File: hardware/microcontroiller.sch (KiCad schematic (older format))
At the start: 14 parts, among them J1 SWD, J2 USB_A, SW1 RESET Switch, U1 STM32L431CBTx, Y1 32.768kHz

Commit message: Finished MC design
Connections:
- net labels added: CP_SHDN_L, Charge_EN, Eh_Sense, MUX1_A0, MUX1_A1, MUX1_EN, MUX2_A0, MUX2_A1, MUX2_EN, Moisture_Sense, Ref_Elec, Temp_Sense
- wire segments 63 -> 79
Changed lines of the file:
@@
 L Device:C_Small C2
 U 1 1 6158D460
-P 3850 3850
-F 0 "C2" H 3900 3950 50  0000 L CNN
-F 1 "20pF" H 3900 3750 50  0000 L CNN
-F 2 "" H 3850 3850 50  0001 C CNN
-F 3 "~" H 3850 3850 50  0001 C CNN
-F 4 "399-C0603C200G4HAC7867CT-ND" H 3850 3850 50  0001 C CNN "Digikey"
-	1    3850 3850
+P 3750 3850
+F 0 "C2" H 3800 3950 50  0000 L CNN
+F 1 "20pF" H 3800 3750 50  0000 L CNN
+F 2 "" H 3750 3850 50  0001 C CNN
+F 3 "~" H 3750 3850 50  0001 C CNN
+F 4 "399-C0603C200G4HAC7867CT-ND" H 3750 3850 50  0001 C CNN "Digikey"
+	1    3750 3850
 	0    1    1    0
 $EndComp
@@
 L Device:C_Small C1
 U 1 1 6158E0B8
-P 3850 3650
-F 0 "C1" H 3750 3750 50  0000 L CNN
-F 1 "20pF" H 3600 3550 50  0000 L CNN
-F 2 "" H 3850 3650 50  0001 C CNN
-F 3 "~" H 3850 3650 50  0001 C CNN
-F 4 "399-C0603C200G4HAC7867CT-ND" H 3850 3650 50  0001 C CNN "Digikey"
-	1    3850 3650
+P 3750 3650
+F 0 "C1" H 3650 3750 50  0000 L CNN
+F 1 "20pF" H 3500 3550 50  0000 L CNN
+F 2 "" H 3750 3650 50  0001 C CNN
+F 3 "~" H 3750 3650 50  0001 C CNN
+F 4 "399-C0603C200G4HAC7867CT-ND" H 3750 3650 50  0001 C CNN "Digikey"
+	1    3750 3650
 	0    1    1    0
 $EndComp
 Wire Wire Line
-	4200 3650 3950 3650
+	4200 3650 3850 3650
 Connection ~ 4200 3650
 Wire Wire Line
-	4200 3850 3950 3850
+	4200 3850 3850 3850
 Connection ~ 4200 3850
 Wire Wire Line
-	3750 3850 3600 3850
-Wire Wire Line
-	3600 3850 3600 3750
-Wire Wire Line
-	3600 3650 3750 3650
+	3650 3850 3500 3850
+Wire Wire Line
+	3500 3850 3500 3750
+Wire Wire Line
+	3500 3650 3650 3650
 $Comp
 L power:GND #PWR06
 U 1 1 6158FD84
-P 3600 3750
-F 0 "#PWR06" H 3600 3500 50  0001 C CNN
-F 1 "GND" V 3605 3622 50  0000 R CNN
-F 2 "" H 3600 3750 50  0001 C CNN
-F 3 "" H 3600 3750 50  0001 C CNN
-	1    3600 3750
+P 3500 3750
+F 0 "#PWR06" H 3500 3500 50  0001 C CNN
+F 1 "GND" V 3505 3622 50  0000 R CNN
+F 2 "" H 3500 3750 50  0001 C CNN
+F 3 "" H 3500 3750 50  0001 C CNN
+	1    3500 3750
 	0    1    1    0
 $EndComp
-Connection ~ 3600 3750
-Wire Wire Line
-	3600 3750 3600 3650
+Connection ~ 3500 3750
+Wire Wire Line
+	3500 3750 3500 3650
 Text Label 5400 2750 2    50   ~ 0
 3V3_VDD
@@
 L Device:LED_Small D1
 U 1 1 6164F04D
-P 6300 4600
-F 0 "D1" H 6300 4835 50  0000 C CNN
-F 1 "Orange" H 6300 4744 50  0000 C CNN
-F 2 "" V 6300 4600 50  0001 C CNN
-F 3 "~" V 6300 4600 50  0001 C CNN
-F 4 "160-1413-1-ND" H 6300 4600 50  0001 C CNN "Digikey"
-	1    6300 4600
-	1    0    0    -1
-$EndComp
-Wire Wire Line
-	6200 4600 6000 4600
+P 4250 4400
+F 0 "D1" H 4250 4200 50  0000 C CNN
+F 1 "Orange" H 4250 4300 50  0000 C CNN
+F 2 "" V 4250 4400 50  0001 C CNN
+F 3 "~" V 4250 4400 50  0001 C CNN
+F 4 "160-1413-1-ND" H 4250 4400 50  0001 C CNN "Digikey"
+	1    4250 4400
+	-1   0    0    -1
+$EndComp
 $Comp
 L Device:R_Small R2
 U 1 1 61650FB5
-P 6700 4600
-F 0 "R2" V 6504 4600 50  0000 C CNN
-F 1 "680" V 6595 4600 50  0000 C CNN
-F 2 "" H 6700 4600 50  0001 C CNN
-F 3 "~" H 6700 4600 50  0001 C CNN
-F 4 "YAG3624CT-ND" V 6700 4600 50  0001 C CNN "Digikey"
-	1    6700 4600
-	0    1    1    0
-$EndComp
-Wire Wire Line
-	6600 4600 6400 4600
+P 3950 4400
+F 0 "R2" V 3850 4400 50  0000 C CNN
+F 1 "680" V 4050 4400 50  0000 C CNN
+F 2 "" H 3950 4400 50  0001 C CNN
+F 3 "~" H 3950 4400 50  0001 C CNN
+F 4 "YAG3624CT-ND" V 3950 4400 50  0001 C CNN "Digikey"
+	1    3950 4400
+	0    -1   -1   0
+$EndComp
+Wire Wire Line
+	4050 4400 4150 4400
 $Comp
 L power:+3V3 #PWR09
 U 1 1 61652B46
-P 6950 4600
-F 0 "#PWR09" H 6950 4450 50  0001 C CNN
-F 1 "+3V3" H 6965 4773 50  0000 C CNN
-F 2 "" H 6950 4600 50  0001 C CNN
-F 3 "" H 6950 4600 50  0001 C CNN
-	1    6950 4600
-	0    1    1    0
-$EndComp
-Wire Wire Line
-	6950 4600 6800 4600
+P 3800 4400
+F 0 "#PWR09" H 3800 4250 50  0001 C CNN
+F 1 "+3V3" H 3815 4573 50  0000 C CNN
+F 2 "" H 3800 4400 50  0001 C CNN
+F 3 "" H 3800 4400 50  0001 C CNN
+	1    3800 4400
+	0    -1   -1   0
+$EndComp
+Wire Wire Line
+	3800 4400 3850 4400
+Text GLabel 6100 4000 2    50   Input ~ 0
+Eh_Sense
+Text GLabel 6100 4100 2    50   Input ~ 0
+Temp_Sense
+Text GLabel 6100 4200 2    50   Input ~ 0
+Ref_Elec
+Text GLabel 6100 4300 2    50   Input ~ 0
+Moisture_Sense
+Text Label 6100 5100 0    50   ~ 0
+USB+
+Text Label 6100 5200 0    50   ~ 0
+USB-
+Wire Wire Line
+	6100 5100 6000 5100
+Wire Wire Line
+	6100 5200 6000 5200
+Text Label 6100 5300 0    50   ~ 0
+SWDIO
+Wire Wire Line
+	6100 5300 6000 5300
+Text Label 6100 5400 0    50   ~ 0
+SWCLK
+Wire Wire Line
+	6100 5400 6000 5400
+Text GLabel 6100 4400 2    50   Input ~ 0
+MUX1_EN
+Text GLabel 6100 4500 2    50   Input ~ 0
+MUX1_A0
+Text GLabel 6100 4600 2    50   Input ~ 0
+MUX1_A1
+Text GLabel 4700 4000 0    50   Input ~ 0
+MUX2_EN
+Wire Wire Line
+	6100 4000 6000 4000
+Wire Wire Line
+	6000 4100 6100 4100
+Wire Wire Line
+	6100 4200 6000 4200
+Wire Wire Line
+	6000 4300 6100 4300
+Wire Wire Line
+	6100 4400 6000 4400
+Wire Wire Line
+	6000 4500 6100 4500
+Wire Wire Line
+	6100 4600 6000 4600
+Text GLabel 4700 4100 0    50   Input ~ 0
+MUX2_A0
+Text GLabel 4700 4200 0    50   Input ~ 0
+MUX2_A1
+Wire Wire Line
+	4700 4000 4800 4000
+Wire Wire Line
+	4800 4100 4700 4100
+Wire Wire Line
+	4700 4200 4800 4200
+Wire Wire Line
+	4350 4400 4800 4400
+Text GLabel 4700 5000 0    50   Input ~ 0
+Charge_EN
+Text GLabel 4700 5100 0    50   Input ~ 0
+CP_SHDN_L
+$Comp
+L power:+5V #PWR?
+U 1 1 6162950C
+P 5600 2800
+F 0 "#PWR?" H 5600 2650 50  0001 C CNN
+F 1 "+5V" H 5615 2973 50  0000 C CNN
+F 2 "" H 5600 2800 50  0001 C CNN
+F 3 "" H 5600 2800 50  0001 C CNN
+	1    5600 2800
+	1    0    0    -1
+$EndComp
+Wire Wire Line
+	4800 5000 4700 5000
+Wire Wire Line
+	4700 5100 4800 5100
 $EndSCHEMATC

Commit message: Added 1V LDO. Added LDO symbol
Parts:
- U1: value STM32L431CBTx -> STM32L4Q5xx
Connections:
- net labels added: +1V0_EN
- wire segments 79 -> 80
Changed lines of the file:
@@
 P 5400 4200
 F 0 "U1" H 6050 5450 50  0000 C CNN
-F 1 "STM32L431CBTx" H 6250 5350 50  0000 C CNN
+F 1 "STM32L4Q5xx" H 6250 5350 50  0000 C CNN
 F 2 "Package_QFP:LQFP-48_7x7mm_P0.5mm" H 4900 2800 50  0001 R CNN
 F 3 "http://www.st.com/st-web-ui/static/active/en/resource/technical/document/datasheet/DM00257211.pdf" H 5400 4200 50  0001 C CNN
@@
 Wire Wire Line
 	4700 5100 4800 5100
+Text GLabel 4700 5200 0    50   Input ~ 0
++1V0_EN
+Wire Wire Line
+	4700 5200 4800 5200
 $EndSCHEMATC

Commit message: Not sure what changes I made sry
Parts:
- added C?: 0.1uF, symbol Device:C_Small
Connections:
- net labels removed: 3V3_VDD
- wire segments 80 -> 84
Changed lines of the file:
@@
 	4950 2300 4950 2350
 Connection ~ 4950 2350
-Wire Wire Line
-	4950 2350 4750 2350
 Connection ~ 4750 2050
 Wire Wire Line
@@
 Wire Wire Line
 	4550 2050 4750 2050
-Text Label 4750 2450 0    50   ~ 0
-3V3_VDD
-Wire Wire Line
-	4750 2450 4750 2350
-Connection ~ 4750 2350
-Wire Wire Line
-	4750 2350 4550 2350
 $Comp
 L Device:R_Small R1
@@
 Wire Wire Line
 	3500 3750 3500 3650
-Text Label 5400 2750 2    50   ~ 0
-3V3_VDD
 Wire Wire Line
 	5400 2800 5400 2750
@@
 F 1 "STM32L4Q5xx" H 6250 5350 50  0000 C CNN
 F 2 "Package_QFP:LQFP-48_7x7mm_P0.5mm" H 4900 2800 50  0001 R CNN
-F 3 "http://www.st.com/st-web-ui/static/active/en/resource/technical/document/datasheet/DM00257211.pdf" H 5400 4200 50  0001 C CNN
+F 3 "https://www.st.com/resource/en/datasheet/stm32l4q5ag.pdf" H 5400 4200 50  0001 C CNN
 F 4 "497-STM32L4Q5CGT6-ND" H 5400 4200 50  0001 C CNN "Digikey"
 	1    5400 4200
@@
 Text GLabel 4700 5100 0    50   Input ~ 0
 CP_SHDN_L
-$Comp
-L power:+5V #PWR?
-U 1 1 6162950C
-P 5600 2800
-F 0 "#PWR?" H 5600 2650 50  0001 C CNN
-F 1 "+5V" H 5615 2973 50  0000 C CNN
-F 2 "" H 5600 2800 50  0001 C CNN
-F 3 "" H 5600 2800 50  0001 C CNN
-	1    5600 2800
-	1    0    0    -1
-$EndComp
 Wire Wire Line
 	4800 5000 4700 5000
@@
 Wire Wire Line
 	4700 5200 4800 5200
+Wire Wire Line
+	4550 2350 4750 2350
+$Comp
+L power:+3V3 #PWR?
+U 1 1 615C7609
+P 5400 2750
+F 0 "#PWR?" H 5400 2600 50  0001 C CNN
+F 1 "+3V3" H 5415 2923 50  0000 C CNN
+F 2 "" H 5400 2750 50  0001 C CNN
+F 3 "" H 5400 2750 50  0001 C CNN
+	1    5400 2750
+	1    0    0    -1
+$EndComp
+$Comp
+L power:GND #PWR?
+U 1 1 615C81D2
+P 4750 2350
+F 0 "#PWR?" H 4750 2100 50  0001 C CNN
+F 1 "GND" H 4755 2177 50  0000 C CNN
+F 2 "" H 4750 2350 50  0001 C CNN
+F 3 "" H 4750 2350 50  0001 C CNN
+	1    4750 2350
+	1    0    0    -1
+$EndComp
+Connection ~ 4750 2350
+Wire Wire Line
+	4750 2350 4950 2350
+$Comp
+L Device:C_Small C?
+U 1 1 615C988A
+P 5550 2200
+F 0 "C?" H 5400 2250 50  0000 L CNN
+F 1 "0.1uF" H 5300 2100 50  0000 L CNN
+F 2 "" H 5550 2200 50  0001 C CNN
+F 3 "~" H 5550 2200 50  0001 C CNN
+F 4 "445-8122-1-ND" H 5550 2200 50  0001 C CNN "Digikey"
+	1    5550 2200
+	1    0    0    -1
+$EndComp
+Wire Wire Line
+	5550 2100 5550 2050
+Wire Wire Line
+	5550 2050 5250 2050
+Connection ~ 5250 2050
+Wire Wire Line
+	5550 2300 5550 2350
+Wire Wire Line
+	5550 2350 5250 2350
+Connection ~ 5250 2350
+Wire Wire Line
+	5600 2800 5500 2800
+Connection ~ 5500 2800
 $EndSCHEMATC

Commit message: House Keeping Tasks
 - Modified parts list parameters for various parts
 - Assigned Ref Des to components
 - Changed TPS717 symbol and feedback resistors
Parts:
- removed C2: 20pF, symbol Device:C_Small
- removed C4, C5, C6, C?: 0.1uF, symbol Device:C_Small
- added C?: 20pF, Capacitor_SMD:C_0603_1608Metric_Pad1.08x0.95mm_HandSolder, symbol Device:C_Small
- added C? (x4): 0.1uF, Capacitor_SMD:C_0603_1608Metric_Pad1.08x0.95mm_HandSolder, symbol Device:C_Small
- C1, C3: footprint (none) -> Capacitor_SMD:C_0603_1608Metric_Pad1.08x0.95mm_HandSolder
- D1: footprint (none) -> Resistor_SMD:R_0805_2012Metric_Pad1.20x1.40mm_HandSolder
- J2: footprint (none) -> Connector_USB:USB3_A_Molex_48393-001; symbol Connector:USB_A -> mallard-rescue:USB_A-Connector
- R1: footprint (none) -> Resistor_SMD:R_0201_0603Metric_Pad0.64x0.40mm_HandSolder
- R2: footprint (none) -> Resistor_SMD:R_0603_1608Metric_Pad0.98x0.95mm_HandSolder
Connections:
- wire segments 84 -> 85
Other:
- note added: "Double check footprint for USB connector"

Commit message: Added more ref des
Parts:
- gave numbers to parts that had none: 5
- renumbered C3 to C400, C1 to C405, R1 to R400, R2 to R401, SW1 to SW400, U1 to U400
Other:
- moved on the sheet: J2

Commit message: Finished adding TMP sensors and footprints
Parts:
- removed J1: SWD, symbol Connector_Generic:Conn_02x05_Odd_Even
- added J2: Conn_02x03_Odd_Even, Connector_PinHeader_1.27mm:PinHeader_2x03_P1.27mm_Vertical, symbol Connector_Generic:Conn_02x03_Odd_Even
- C1: renamed from C405; symbol Device:C_Small -> mallard-rescue:C_Small-Device
- C2: renamed from C400; symbol Device:C_Small -> mallard-rescue:C_Small-Device
- C3: renamed from C401; symbol Device:C_Small -> mallard-rescue:C_Small-Device
- C4: renamed from C406; symbol Device:C_Small -> mallard-rescue:C_Small-Device
- C5: renamed from C402; symbol Device:C_Small -> mallard-rescue:C_Small-Device
- C6: renamed from C403; symbol Device:C_Small -> mallard-rescue:C_Small-Device
- C7: renamed from C404; symbol Device:C_Small -> mallard-rescue:C_Small-Device
- D1: symbol Device:LED_Small -> mallard-rescue:LED_Small-Device
- R1: renamed from R401; symbol Device:R_Small -> mallard-rescue:R_Small-Device
- R2: renamed from R400; symbol Device:R_Small -> mallard-rescue:R_Small-Device
- SW1: renamed from SW400; footprint (none) -> Button_Switch_SMD:SW_SPST_B3U-1000P; symbol Switch:SW_Push_Open_Dual -> mallard-rescue:SW_Push_Open_Dual-Switch; Digikey (none) -> SW1020CT-ND
- U1: renamed from U400; symbol MCU_ST_STM32L4:STM32L431CBTx -> mallard-rescue:STM32L431CBTx-MCU_ST_STM32L4
- Y1: symbol Device:Crystal_Small -> mallard-rescue:Crystal_Small-Device
- renumbered J2 to J3
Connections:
- wire segments 85 -> 83
- no-connect marks 3 -> 1
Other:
- note added: "I have these switches on hand"
- note added: "Programming connector copied from a previous project (Flamingo)"

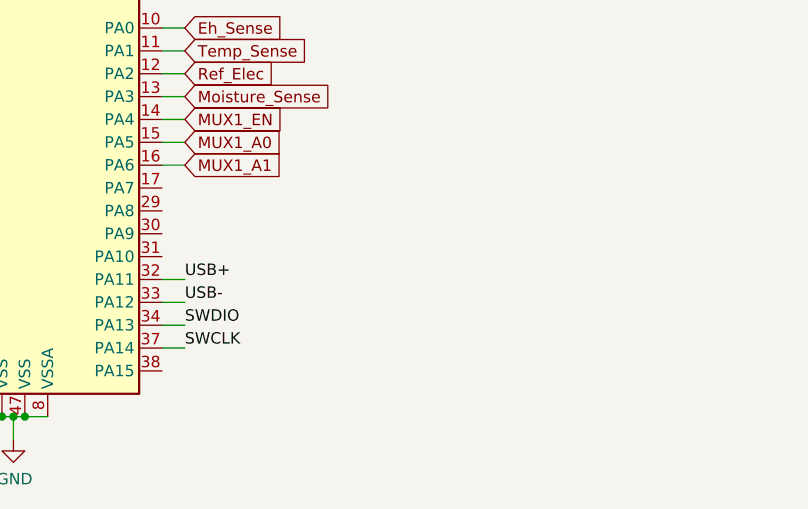
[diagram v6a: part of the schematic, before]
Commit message: Added UART connector on STM32
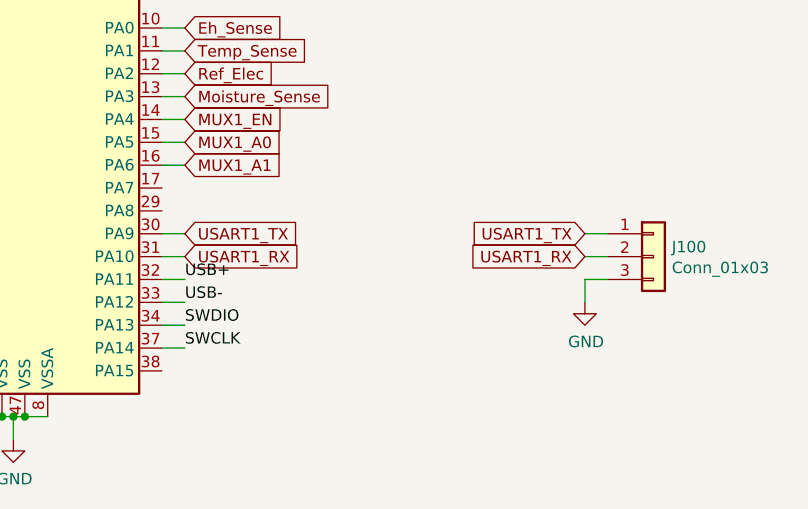
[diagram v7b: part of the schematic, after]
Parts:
- added J100: Conn_01x03, Connector_PinHeader_2.54mm:PinHeader_1x03_P2.54mm_Vertical_SMD_Pin1Right, symbol Connector_Generic:Conn_01x03
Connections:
- net GND: now also J100.3 (Pin_3)
- net USART1_TX: now reaches U1.30 (PA9)
- net USART1_TX: now also J100.1 (Pin_1)
- net USART1_RX: now reaches U1.31 (PA10)
- net USART1_RX: now also J100.2 (Pin_2)
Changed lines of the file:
@@
 $Descr A4 11693 8268
 encoding utf-8
-Sheet 2 4
+Sheet 1 1
 Title ""
 Date ""
@@
 Text Notes 6650 1950 0    50   ~ 0
 I have these switches on hand
+Wire Wire Line
+	6550 5950 6650 5950
+Text GLabel 6650 5850 2    50   Input ~ 0
+USART1_TX
+Text GLabel 6650 5950 2    50   Input ~ 0
+USART1_RX
+Wire Wire Line
+	6550 5850 6650 5850
+Wire Wire Line
+	8500 5950 8400 5950
+Text GLabel 8400 5850 0    50   Input ~ 0
+USART1_TX
+Text GLabel 8400 5950 0    50   Input ~ 0
+USART1_RX
+Wire Wire Line
+	8500 5850 8400 5850
+$Comp
+L Connector_Generic:Conn_01x03 J100
+U 1 1 61EA675F
+P 8700 5950
+F 0 "J100" H 8780 5992 50  0000 L CNN
+F 1 "Conn_01x03" H 8780 5901 50  0000 L CNN
+F 2 "Connector_PinHeader_2.54mm:PinHeader_1x03_P2.54mm_Vertical_SMD_Pin1Right" H 8700 5950 50  0001 C CNN
+F 3 "https://drawings-pdf.s3.amazonaws.com/11657.pdf" H 8700 5950 50  0001 C CNN
+F 4 "S1013EC-03-ND" H 8700 5950 50  0001 C CNN "Digikey"
+	1    8700 5950
+	1    0    0    -1
+$EndComp
+Wire Wire Line
+	8400 6050 8400 6150
+$Comp
+L mallard-rescue:GND-power #PWR?
+U 1 1 61EAAB16
+P 8400 6150
+F 0 "#PWR?" H 8400 5900 50  0001 C CNN
+F 1 "GND" H 8405 5977 50  0000 C CNN
+F 2 "" H 8400 6150 50  0001 C CNN
+F 3 "" H 8400 6150 50  0001 C CNN
+	1    8400 6150
+	1    0    0    -1
+$EndComp
+Wire Wire Line
+	8500 6050 8400 6050
 $EndSCHEMATC
